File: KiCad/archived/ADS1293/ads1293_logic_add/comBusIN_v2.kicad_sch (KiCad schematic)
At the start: 1 part, among them J2 XF2J-1824-12A

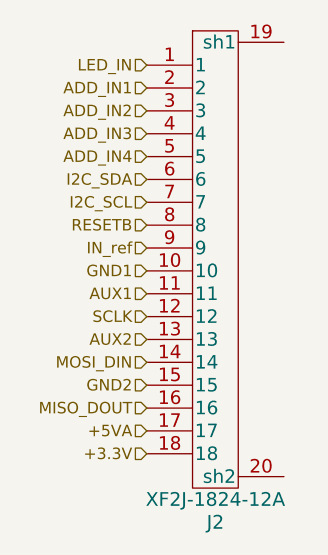
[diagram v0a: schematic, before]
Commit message: renamed SPI buses
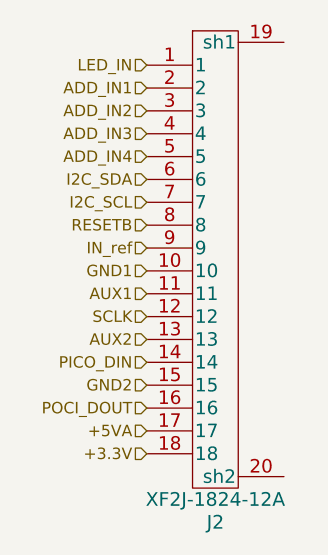
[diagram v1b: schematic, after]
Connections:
- net MISO_DOUT renamed POCI_DOUT
- net MOSI_DIN renamed PICO_DIN
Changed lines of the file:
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@@
     (effects (font (size 1.27 1.27)) (justify right))
   )
-  (hierarchical_label "MISO_DOUT" (shape input) (at 113.03 116.84 180) (fields_autoplaced)
+  (hierarchical_label "POCI_DOUT" (shape input) (at 113.03 116.84 180) (fields_autoplaced)
     (effects (font (size 1.27 1.27)) (justify right))
   )
@@
     (effects (font (size 1.27 1.27)) (justify right))
   )
-  (hierarchical_label "MOSI_DIN" (shape input) (at 113.03 111.76 180) (fields_autoplaced)
+  (hierarchical_label "PICO_DIN" (shape input) (at 113.03 111.76 180) (fields_autoplaced)
     (effects (font (size 1.27 1.27)) (justify right))
   )
